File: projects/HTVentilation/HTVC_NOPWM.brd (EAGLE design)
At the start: 80.6 x 58.1 mm, 71 parts

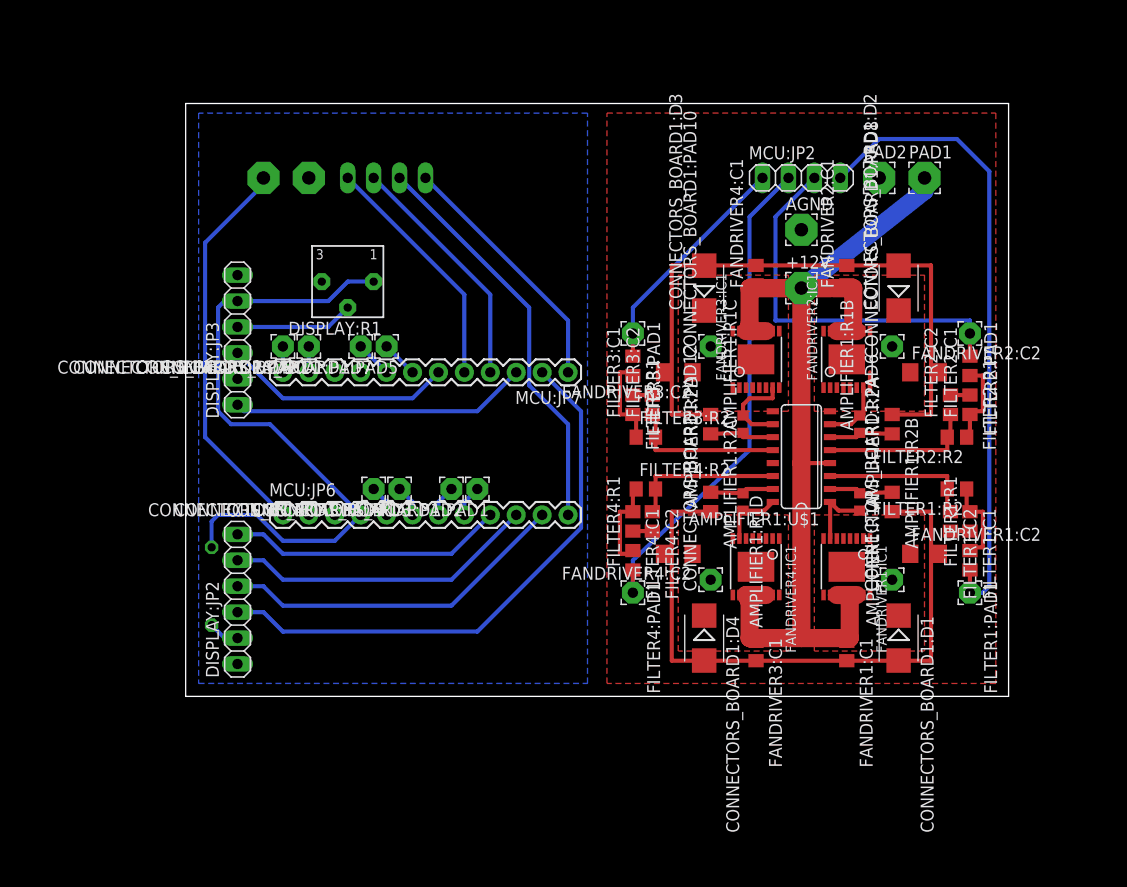
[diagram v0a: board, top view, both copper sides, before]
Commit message: added no smd version
through hole non temperature controlled version
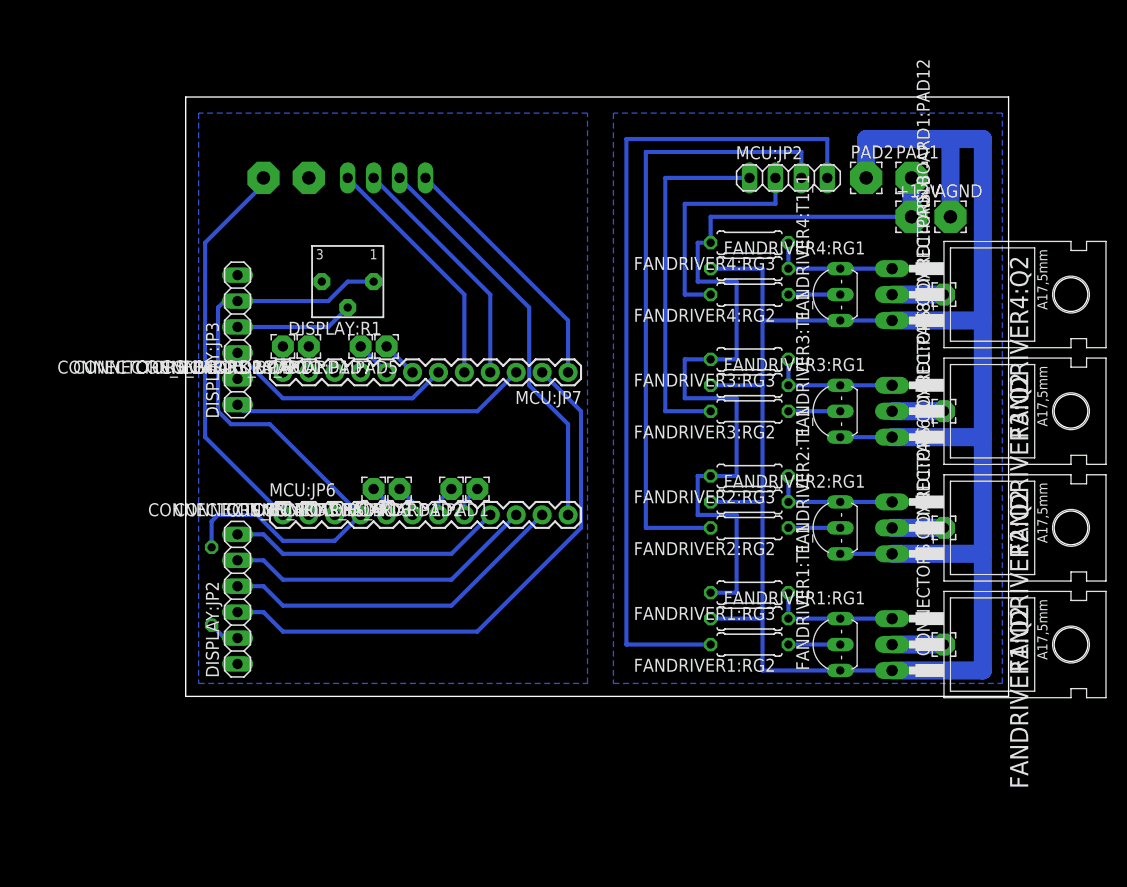
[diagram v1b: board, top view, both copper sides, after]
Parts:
- removed AMPLIFIER1:R1A, AMPLIFIER1:R1B, AMPLIFIER1:R1C, AMPLIFIER1:R1D: 14K, rcl:R0603
- removed AMPLIFIER1:R2A, AMPLIFIER1:R2B, AMPLIFIER1:R2C, AMPLIFIER1:R2D: 10K, resistor:R0805
- removed AMPLIFIER1:U$1: LT1014, nervus:SO16
- removed CONNECTORS_BOARD1:D1, CONNECTORS_BOARD1:D2, CONNECTORS_BOARD1:D3, CONNECTORS_BOARD1:D4: MBRS240LT3, nervus:SMB-403A
- removed FANDRIVER1:C1, FANDRIVER2:C1, FANDRIVER3:C1, FANDRIVER4:C1: 2.2uF, rcl:C0805
- removed FANDRIVER1:C2, FANDRIVER2:C2, FANDRIVER3:C2, FANDRIVER4:C2: 10uF, rcl:C1206
- removed FANDRIVER1:IC1, FANDRIVER2:IC1, FANDRIVER3:IC1, FANDRIVER4:IC1: LT3083EFE, nervus:TSSOP16EXP
- removed FILTER1:C1, FILTER1:C2, FILTER2:C1, FILTER2:C2, FILTER3:C1, FILTER3:C2, FILTER4:C1, FILTER4:C2: 100n, resistor:C0805
- removed FILTER1:PAD1, FILTER2:PAD1, FILTER3:PAD1, FILTER4:PAD1: (no value), wirepad:2,15/1,0
- removed FILTER1:R1, FILTER1:R2, FILTER2:R1, FILTER2:R2, FILTER3:R1, FILTER3:R2, FILTER4:R1, FILTER4:R2: 100K, resistor:R0805
- added FANDRIVER1:Q2, FANDRIVER2:Q2, FANDRIVER3:Q2, FANDRIVER4:Q2: IRF510, transistor-fet:TO220
- added FANDRIVER1:RG1, FANDRIVER1:RG3, FANDRIVER2:RG1, FANDRIVER2:RG3, FANDRIVER3:RG1, FANDRIVER3:RG3, FANDRIVER4:RG1, FANDRIVER4:RG3: 10K, rcl:0207/7
- added FANDRIVER1:RG2, FANDRIVER2:RG2, FANDRIVER3:RG2, FANDRIVER4:RG2: 1K, rcl:0207/7
- added FANDRIVER1:T1_1, FANDRIVER2:T1_1, FANDRIVER3:T1_1, FANDRIVER4:T1_1: 2N2222, adafruit:TO92-EBC-OVAL
- moved CONNECTORS_BOARD1:PAD12 36.1 mm to (74.3, 39.4)
- moved CONNECTORS_BOARD1:PAD10 23.7 mm to (74.3, 27.9)
- moved CONNECTORS_BOARD1:PAD8 18.5 mm to (74.3, 16.5)
- moved AGND 14.7 mm to (74.9, 47.0)
- moved +12V 12.9 mm to (71.1, 47.0)
- moved CONNECTORS_BOARD1:PAD6 8.13 mm to (74.3, 5.08)
- moved MCU:JP2 1.27 mm to (59.1, 50.8)
- moved PAD1 1.27 mm to (71.1, 50.8)
- moved PAD2 1.27 mm to (66.7, 50.8)
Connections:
- removed net AMPLIFIER1:N$1: AMPLIFIER1:R1B.1, AMPLIFIER1:R2B.2, AMPLIFIER1:U$1.6
- removed net AMPLIFIER1:N$2: AMPLIFIER1:R1C.1, AMPLIFIER1:R2C.2, AMPLIFIER1:U$1.11
- removed net AMPLIFIER1:N$3: AMPLIFIER1:R1D.1, AMPLIFIER1:R2D.2, AMPLIFIER1:U$1.15
- removed net AMPLIFIER1:N$9: AMPLIFIER1:R1A.1, AMPLIFIER1:R2A.2, AMPLIFIER1:U$1.2
- removed net FILTER1:N$8: FILTER1:C1.1, FILTER1:R1.2, FILTER1:R2.1
- removed net FILTER2:N$8: FILTER2:C1.1, FILTER2:R1.2, FILTER2:R2.1
- removed net FILTER3:N$8: FILTER3:C1.1, FILTER3:R1.2, FILTER3:R2.1
- removed net FILTER4:N$8: FILTER4:C1.1, FILTER4:R1.2, FILTER4:R2.1
- removed net N$45: AMPLIFIER1:U$1.3, FILTER1:C2.1, FILTER1:R2.2
- removed net N$46: AMPLIFIER1:U$1.5, FILTER2:C2.1, FILTER2:R2.2
- removed net N$47: AMPLIFIER1:U$1.12, FILTER3:C2.1, FILTER3:R2.2
- removed net N$48: AMPLIFIER1:U$1.14, FILTER4:C2.1, FILTER4:R2.2
- removed net N$49: AMPLIFIER1:R1A.2, AMPLIFIER1:U$1.1, FANDRIVER1:IC1.7
- removed net N$50: AMPLIFIER1:R1B.2, AMPLIFIER1:U$1.7, FANDRIVER2:IC1.7
- removed net N$51: AMPLIFIER1:R1C.2, AMPLIFIER1:U$1.10, FANDRIVER3:IC1.7
- removed net N$52: AMPLIFIER1:R1D.2, AMPLIFIER1:U$1.16, FANDRIVER4:IC1.7
- new net FANDRIVER1:N$10: FANDRIVER1:RG2.1, FANDRIVER1:T1_1.B
- new net FANDRIVER1:N$15: FANDRIVER1:Q2.1, FANDRIVER1:RG1.2, FANDRIVER1:RG3.1, FANDRIVER1:T1_1.C
- new net FANDRIVER2:N$10: FANDRIVER2:RG2.1, FANDRIVER2:T1_1.B
- new net FANDRIVER2:N$15: FANDRIVER2:Q2.1, FANDRIVER2:RG1.2, FANDRIVER2:RG3.1, FANDRIVER2:T1_1.C
- new net FANDRIVER3:N$10: FANDRIVER3:RG2.1, FANDRIVER3:T1_1.B
- new net FANDRIVER3:N$15: FANDRIVER3:Q2.1, FANDRIVER3:RG1.2, FANDRIVER3:RG3.1, FANDRIVER3:T1_1.C
- new net FANDRIVER4:N$10: FANDRIVER4:RG2.1, FANDRIVER4:T1_1.B
- new net FANDRIVER4:N$15: FANDRIVER4:Q2.1, FANDRIVER4:RG1.2, FANDRIVER4:RG3.1, FANDRIVER4:T1_1.C
- net AGND: now also FANDRIVER1:Q2.3, FANDRIVER1:RG1.1, FANDRIVER1:T1_1.E, FANDRIVER2:Q2.3, FANDRIVER2:RG1.1, FANDRIVER2:T1_1.E, FANDRIVER3:Q2.3, FANDRIVER3:RG1.1, FANDRIVER3:T1_1.E, FANDRIVER4:Q2.3, FANDRIVER4:RG1.1, FANDRIVER4:T1_1.E; no longer AMPLIFIER1:R2A.1, AMPLIFIER1:R2B.1, AMPLIFIER1:R2C.1, AMPLIFIER1:R2D.1, AMPLIFIER1:U$1.13, CONNECTORS_BOARD1:D1.A, CONNECTORS_BOARD1:D2.A, CONNECTORS_BOARD1:D3.A, CONNECTORS_BOARD1:D4.A, FANDRIVER1:C1.2, FANDRIVER1:C2.2, FANDRIVER2:C1.2, FANDRIVER2:C2.2, FANDRIVER3:C1.2, FANDRIVER3:C2.2, FANDRIVER4:C1.2, FANDRIVER4:C2.2, FILTER1:C1.2, FILTER1:C2.2, FILTER2:C1.2, FILTER2:C2.2, FILTER3:C1.2, FILTER3:C2.2, FILTER4:C1.2, FILTER4:C2.2
- net N$10: now also FANDRIVER3:Q2.2; no longer CONNECTORS_BOARD1:D3.C, FANDRIVER3:C2.1, FANDRIVER3:IC1.1, FANDRIVER3:IC1.16, FANDRIVER3:IC1.2, FANDRIVER3:IC1.3, FANDRIVER3:IC1.4, FANDRIVER3:IC1.5, FANDRIVER3:IC1.6, FANDRIVER3:IC1.8, FANDRIVER3:IC1.9, FANDRIVER3:IC1.EXP
- net N$11: now also FANDRIVER2:Q2.2; no longer CONNECTORS_BOARD1:D2.C, FANDRIVER2:C2.1, FANDRIVER2:IC1.1, FANDRIVER2:IC1.16, FANDRIVER2:IC1.2, FANDRIVER2:IC1.3, FANDRIVER2:IC1.4, FANDRIVER2:IC1.5, FANDRIVER2:IC1.6, FANDRIVER2:IC1.8, FANDRIVER2:IC1.9, FANDRIVER2:IC1.EXP
- net N$12: now also FANDRIVER1:Q2.2; no longer CONNECTORS_BOARD1:D1.C, FANDRIVER1:C2.1, FANDRIVER1:IC1.1, FANDRIVER1:IC1.16, FANDRIVER1:IC1.2, FANDRIVER1:IC1.3, FANDRIVER1:IC1.4, FANDRIVER1:IC1.5, FANDRIVER1:IC1.6, FANDRIVER1:IC1.8, FANDRIVER1:IC1.9, FANDRIVER1:IC1.EXP
- net N$21: now also FANDRIVER1:RG2.2; no longer FILTER1:PAD1.1, FILTER1:R1.1
- net N$22: now also FANDRIVER2:RG2.2; no longer FILTER2:PAD1.1, FILTER2:R1.1
- net N$23: now also FANDRIVER3:RG2.2; no longer FILTER3:PAD1.1, FILTER3:R1.1
- net N$37: now also FANDRIVER4:RG2.2; no longer FILTER4:PAD1.1, FILTER4:R1.1
- net N$9: now also FANDRIVER4:Q2.2; no longer CONNECTORS_BOARD1:D4.C, FANDRIVER4:C2.1, FANDRIVER4:IC1.1, FANDRIVER4:IC1.16, FANDRIVER4:IC1.2, FANDRIVER4:IC1.3, FANDRIVER4:IC1.4, FANDRIVER4:IC1.5, FANDRIVER4:IC1.6, FANDRIVER4:IC1.8, FANDRIVER4:IC1.9, FANDRIVER4:IC1.EXP
- net VCC: now also FANDRIVER1:RG3.2, FANDRIVER2:RG3.2, FANDRIVER3:RG3.2, FANDRIVER4:RG3.2; no longer AMPLIFIER1:U$1.4, FANDRIVER1:C1.1, FANDRIVER1:IC1.10, FANDRIVER1:IC1.11, FANDRIVER1:IC1.12, FANDRIVER1:IC1.13, FANDRIVER1:IC1.14, FANDRIVER1:IC1.15, FANDRIVER2:C1.1, FANDRIVER2:IC1.10, FANDRIVER2:IC1.11, FANDRIVER2:IC1.12, FANDRIVER2:IC1.13, FANDRIVER2:IC1.14, FANDRIVER2:IC1.15, FANDRIVER3:C1.1, FANDRIVER3:IC1.10, FANDRIVER3:IC1.11, FANDRIVER3:IC1.12, FANDRIVER3:IC1.13, FANDRIVER3:IC1.14, FANDRIVER3:IC1.15, FANDRIVER4:C1.1, FANDRIVER4:IC1.10, FANDRIVER4:IC1.11, FANDRIVER4:IC1.12, FANDRIVER4:IC1.13, FANDRIVER4:IC1.14, FANDRIVER4:IC1.15
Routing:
- net AGND: track 132.8 -> 205.7 mm
- net N$37: track 89.2 -> 62.7 mm
- net N$22: track 61.9 -> 84.7 mm
- net VCC: track 145.9 -> 124.3 mm
- net N$21: track 86.3 -> 105.1 mm
- net N$46: track 15.6 -> 0.00 mm
- net N$48: track 15.3 -> 0.00 mm
- net N$45: track 15.1 -> 0.00 mm
- net N$47: track 15.1 -> 0.00 mm
- net N$23: track 47.6 -> 60.4 mm
- net FANDRIVER4:N$15: track 0.00 -> 12.7 mm
- net FANDRIVER3:N$15: track 0.00 -> 12.7 mm
- net FANDRIVER2:N$15: track 0.00 -> 12.7 mm
- net FANDRIVER1:N$15: track 0.00 -> 12.7 mm
- net FILTER3:N$8: track 9.97 -> 0.00 mm
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- removed copper zone on layer 1, net AGND
- removed copper zone on layer 1, net N$10
- removed copper zone on layer 1, net N$11
- removed copper zone on layer 1, net N$12
- removed copper zone on layer 1, net N$9
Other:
- board size 80.6 x 58.1 mm -> 80.6 x 58.7 mm

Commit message: new items in the lib + new 4 layer board
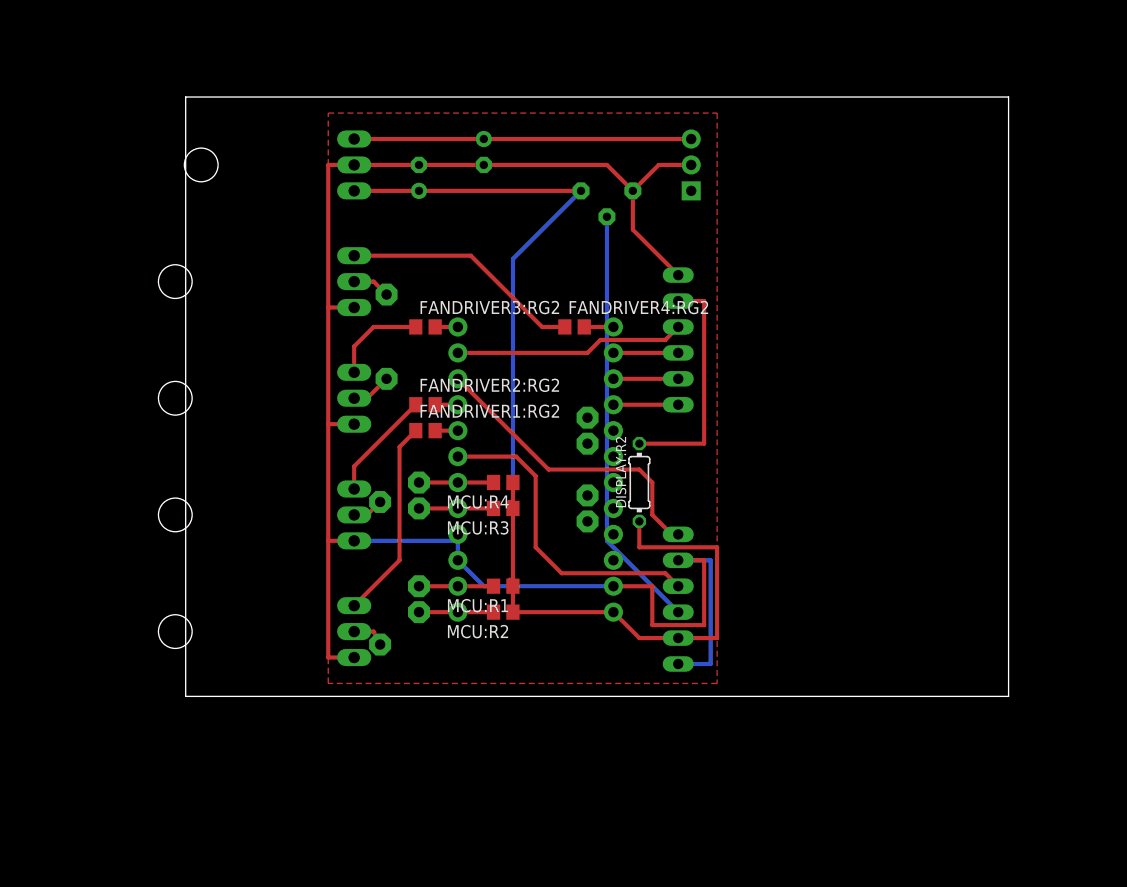
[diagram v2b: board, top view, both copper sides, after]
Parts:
- removed +12V, +12V1, AGND, AGND9, PAD1, PAD2: (no value), wirepad:3,17/1,3
- removed FANDRIVER1:Q2, FANDRIVER2:Q2, FANDRIVER3:Q2, FANDRIVER4:Q2: IRF510, transistor-fet:TO220
- removed FANDRIVER1:RG1, FANDRIVER1:RG3, FANDRIVER2:RG1, FANDRIVER2:RG3, FANDRIVER3:RG1, FANDRIVER3:RG3, FANDRIVER4:RG1, FANDRIVER4:RG3: 10K, rcl:0207/7
- removed MCU:JP1, MCU:JP2: (no value), pinhead:1X04
- added C1: 0.33uF, rcl:E2,5-6
- added C2: 0.1uF, rcl:E2,5-6
- added IC1: 7805T, linear:TO220H
- added JP1: (no value), SparkFun-Connectors:MOLEX-1X3
- added MCU:R1, MCU:R2, MCU:R3, MCU:R4: 10K, rcl:R0805
- FANDRIVER1:RG2, FANDRIVER2:RG2, FANDRIVER3:RG2, FANDRIVER4:RG2: device rcl:0207/7 -> rcl:R0805
- FANDRIVER1:T1_1, FANDRIVER2:T1_1, FANDRIVER3:T1_1, FANDRIVER4:T1_1: value 2N2222 -> TIP120; device adafruit:TO92-EBC-OVAL -> transistor-power:TO220AH
- moved CONNECTORS_BOARD1:PAD8 55.3 mm to (19.1, 19.1), flipped to the bottom
- moved CONNECTORS_BOARD1:PAD6 55.2 mm to (19.1, 5.08), flipped to the bottom
- moved CONNECTORS_BOARD1:PAD10 54.7 mm to (19.7, 31.1), flipped to the bottom
- moved CONNECTORS_BOARD1:PAD12 54.6 mm to (19.7, 39.4), flipped to the bottom
- moved FANDRIVER1:T1_1 52.7 mm to (10.2, 6.35), flipped to the bottom, turned to 270 degrees
- moved FANDRIVER2:T1_1 52.7 mm to (10.2, 17.8), flipped to the bottom, turned to 270 degrees
- moved FANDRIVER3:T1_1 52.7 mm to (10.2, 29.2), flipped to the bottom, turned to 270 degrees
- moved FANDRIVER4:T1_1 52.7 mm to (10.2, 40.6), flipped to the bottom, turned to 270 degrees
- moved DISPLAY:JP2 50.1 mm to (48.3, 34.9), flipped to the bottom, turned to 270 degrees
- moved DISPLAY:JP3 50.1 mm to (48.3, 9.53), flipped to the bottom, turned to 270 degrees
- moved DISPLAY:R2 43.1 mm to (44.5, 21.0), flipped to the top, turned to 90 degrees
- moved FANDRIVER1:RG2 38.0 mm to (23.5, 26.0), turned to 0 degrees
- moved FANDRIVER2:RG2 34.0 mm to (23.5, 28.6), turned to 0 degrees
- moved MCU:JP6 33.8 mm to (41.9, 8.26), flipped to the bottom, turned to 90 degrees
- moved FANDRIVER3:RG2 32.8 mm to (23.5, 36.2), turned to 0 degrees
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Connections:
- removed net FANDRIVER1:N$15: FANDRIVER1:Q2.1, FANDRIVER1:RG1.2, FANDRIVER1:RG3.1, FANDRIVER1:T1_1.C
- removed net FANDRIVER2:N$15: FANDRIVER2:Q2.1, FANDRIVER2:RG1.2, FANDRIVER2:RG3.1, FANDRIVER2:T1_1.C
- removed net FANDRIVER3:N$15: FANDRIVER3:Q2.1, FANDRIVER3:RG1.2, FANDRIVER3:RG3.1, FANDRIVER3:T1_1.C
- removed net FANDRIVER4:N$15: FANDRIVER4:Q2.1, FANDRIVER4:RG1.2, FANDRIVER4:RG3.1, FANDRIVER4:T1_1.C
- new net MCU:5VOUT: MCU:JP6.4
- net +5V: now also C2.+, IC1.3, MCU:JP6.1, MCU:R1.1, MCU:R2.1, MCU:R3.1, MCU:R4.1; no longer MCU:JP6.4
- net AGND: now also C1.-, C2.-, IC1.2, JP1.2; no longer AGND.1, AGND9.1, FANDRIVER1:Q2.3, FANDRIVER1:RG1.1, FANDRIVER2:Q2.3, FANDRIVER2:RG1.1, FANDRIVER3:Q2.3, FANDRIVER3:RG1.1, FANDRIVER4:Q2.3, FANDRIVER4:RG1.1, PAD2.1
- net N$10: now also FANDRIVER3:T1_1.C; no longer FANDRIVER3:Q2.2
- net N$11: now also FANDRIVER2:T1_1.C; no longer FANDRIVER2:Q2.2
- net N$12: now also FANDRIVER1:T1_1.C; no longer FANDRIVER1:Q2.2
- net N$21: no longer MCU:JP1.4, MCU:JP2.4
- net N$22: no longer MCU:JP1.3, MCU:JP2.3
- net N$23: no longer MCU:JP1.1, MCU:JP2.1
- net N$37: no longer MCU:JP1.2, MCU:JP2.2
- net N$9: now also FANDRIVER4:T1_1.C; no longer FANDRIVER4:Q2.2
- net TACH0: now also MCU:R4.2
- net TACH1: now also MCU:R3.2
- net TACH2: now also MCU:R2.2
- net TACH3: now also MCU:R1.2
- net VCC: now also C1.+, IC1.1, JP1.3; no longer +12V.1, +12V1.1, FANDRIVER1:RG3.2, FANDRIVER2:RG3.2, FANDRIVER3:RG3.2, FANDRIVER4:RG3.2, MCU:JP6.1, PAD1.1
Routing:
- net N$21: track 105.1 -> 2.23 mm
- net VCC: track 124.3 -> 33.0 mm
- net N$22: track 84.7 -> 2.23 mm
- net N$37: track 62.7 -> 2.86 mm
- net N$23: track 60.4 -> 2.23 mm
- net +5V: track 64.1 -> 110.1 mm
- net N$6: track 55.5 -> 22.6 mm
- net AGND: track 205.7 -> 173.9 mm
- net DISPLAY:N$1: track 11.6 -> 41.6 mm
- net N$5: track 34.3 -> 6.35 mm
- net N$4: track 30.7 -> 6.35 mm
- net N$3: track 27.1 -> 6.35 mm
- net DISPLAY:N$2: track 3.07 -> 22.9 mm
- net FANDRIVER4:N$10: track 5.08 -> 23.5 mm
- net FANDRIVER1:N$10: track 5.08 -> 19.6 mm
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- added copper zone on layer 1, net _GND
- removed copper zone on layer 16, net AGND
